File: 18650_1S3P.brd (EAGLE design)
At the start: 94 x 67.7 mm, 27 parts, among them Q1 DMG3404, Q2 DMG3404, Q3 DMG3404, Q4 DMG3404

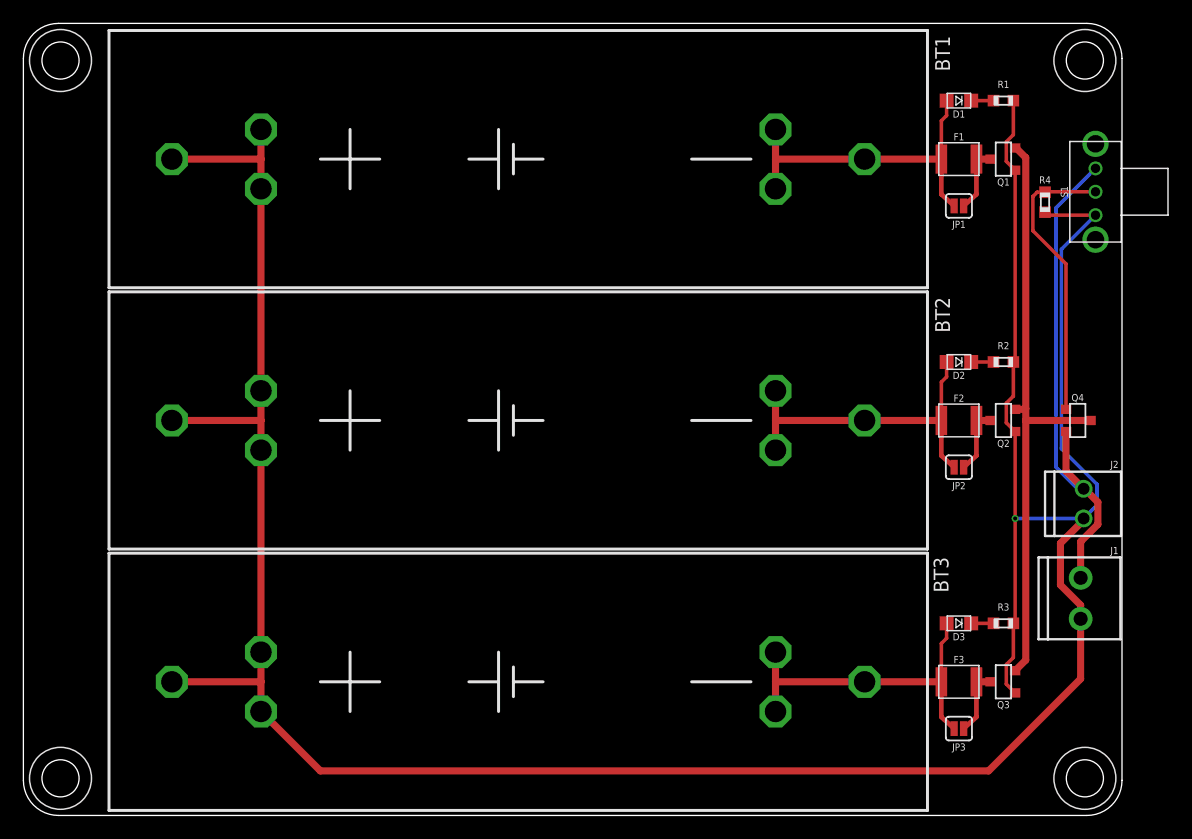
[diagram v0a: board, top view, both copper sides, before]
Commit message: Update for v0.1 system
Updated system to v0.1, changed switching and reverse polarity protection system, ready for fab
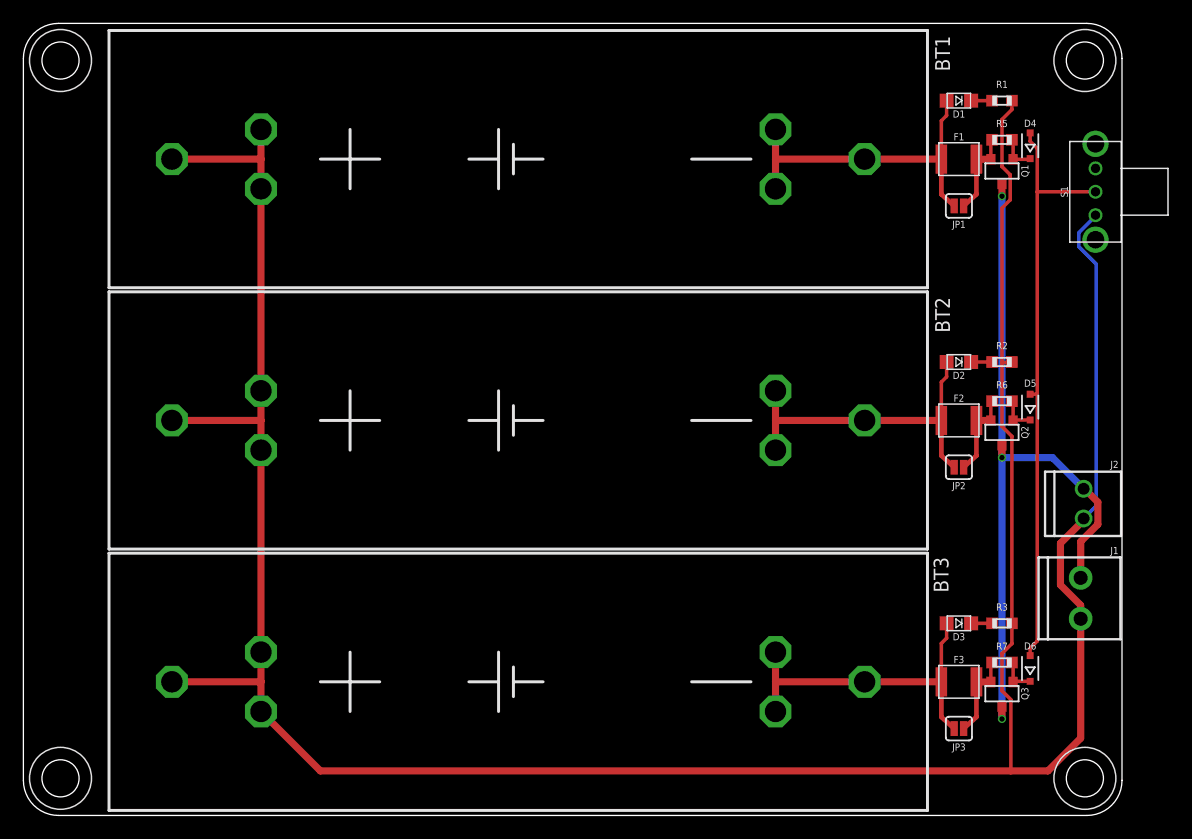
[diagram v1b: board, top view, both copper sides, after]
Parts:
- removed Q4: DMG3404, bschulz:SOT23-3
- removed R4: 10M, bschulz_passives:R0603
- added D4, D5, D6: 1N4148, bschulz:SOD323-R
- added R5, R6, R7: 100k, bschulz_passives:R0603
- moved Q3 1.02 mm to (77.3, 10.4), turned to 180 degrees
- moved Q1 1.02 mm to (77.3, 55.1), turned to 180 degrees
- moved Q2 1.02 mm to (77.3, 32.8), turned to 180 degrees
- moved R1 0.13 mm to (77.3, 61.1)
- moved R2 0.13 mm to (77.3, 38.8)
- moved R3 0.13 mm to (77.3, 16.4)
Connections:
- removed net N$7: Q4.1, R4.1, S1.2
- removed net PACK-: Q1.2, Q2.2, Q3.2, Q4.3
- new net GATE: D4.A, D5.A, D6.A, S1.2
- new net N$10: D4.C, Q1.1, R5.2
- new net N$11: D6.C, Q3.1, R7.2
- new net N$9: D5.C, Q2.1, R6.2
- net N$3: now also Q1.2, R5.1; no longer Q1.3
- net N$4: now also Q2.2, R6.1; no longer Q2.3
- net N$6: now also Q3.2, R7.1; no longer Q3.3
- net SYS+: no longer Q1.1, Q2.1, Q3.1, R4.2
- net SYS-: now also Q1.3, Q2.3, Q3.3; no longer Q4.2, S1.3
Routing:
- net PACK-: track 52.0 -> 0.00 mm
- net GATE: track 0.00 -> 50.8 mm
- net N$7: track 24.9 -> 0.00 mm
- net SYS-: track 44.4 -> 64.7 mm, vias 0 -> 3
- net N$9: track 0.00 -> 3.20 mm
- net N$11: track 0.00 -> 3.20 mm
- net N$10: track 0.00 -> 3.20 mm
- net N$4: track 5.69 -> 7.43 mm
- net N$6: track 5.69 -> 7.43 mm
- net N$3: track 5.69 -> 7.43 mm
- net SYS+: track 255.0 -> 254.3 mm, vias 1 -> 0
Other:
- board text added: "1S3P - 18650 Project Gonk Bobby Schulz v0.1"
- board text removed: "Triple Battery Holder 18650 Bobby Schulz v0.0"
